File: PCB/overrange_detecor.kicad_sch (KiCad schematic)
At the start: 21 parts, among them Q105 BC807, Q301 BC807, U101 74HC00, U106 TLV3542, U7 TLV3542

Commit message: footprints
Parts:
- removed U106, U7: TLV3542, w-ic:SOIC-8, symbol w-analog-ic:TLV3542
- added C302: 100n, Capacitor_SMD:C_0603_1608Metric, symbol Device:C
- added U301: TLV3542, w-ic:SOIC-8, symbol w-analog-ic:TLV3542
- added U303: LM321, w-ic:SOT-23-5L, symbol w-analog-ic:LM321
- C301: renamed from C14; footprint (none) -> Capacitor_SMD:C_0603_1608Metric
- D301: footprint (none) -> LED_SMD:LED_0603_1608Metric
- R301: renamed from R110; footprint (none) -> Resistor_SMD:R_0603_1608Metric
- R302: renamed from R111; footprint (none) -> Resistor_SMD:R_0603_1608Metric
- R303: renamed from R113; footprint (none) -> Resistor_SMD:R_0603_1608Metric
- R304: renamed from R114; footprint (none) -> Resistor_SMD:R_0603_1608Metric
- R305: renamed from R112; footprint (none) -> Resistor_SMD:R_0603_1608Metric
- R306: renamed from R115; footprint (none) -> Resistor_SMD:R_0603_1608Metric
- R307: renamed from R301; footprint (none) -> Resistor_SMD:R_0603_1608Metric
- R308: renamed from R304; footprint (none) -> Resistor_SMD:R_0603_1608Metric
- R309: renamed from R302; footprint (none) -> Resistor_SMD:R_0603_1608Metric
- R310: renamed from R303; footprint (none) -> Resistor_SMD:R_0603_1608Metric
- R311: renamed from R5; footprint (none) -> Resistor_SMD:R_0603_1608Metric
- R312: renamed from R116; footprint (none) -> Resistor_SMD:R_0603_1608Metric
- R313: renamed from R4; footprint (none) -> Resistor_SMD:R_0603_1608Metric
- R314: renamed from R305; footprint (none) -> Resistor_SMD:R_0603_1608Metric
- U302: renamed from U101; footprint (none) -> w-ic:SOIC-14 208mil
- renumbered Q105 to Q301, Q301 to Q302
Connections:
- net +5V: now also C302.1, U303.2 (V-)
- net GND: now also C302.2, U303.5 (V+)
- net GNDA: now also U301.5 (+)
- net at D301.1 (K), R312.2, R313.1: now also U303.4
- net at C301.1, R309.2, R310.2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: now also U303.3 (-)
- net at R311.2, R313.2: now also U303.1 (+)
- net at R302.2, R304.1: now also U301.7
- net at R301.2, R302.1: now also U301.6 (-)
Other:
- moved on the sheet: C301, D301, Q301, Q302, R301, R302, R303, R304, R305, R306, R307, R308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

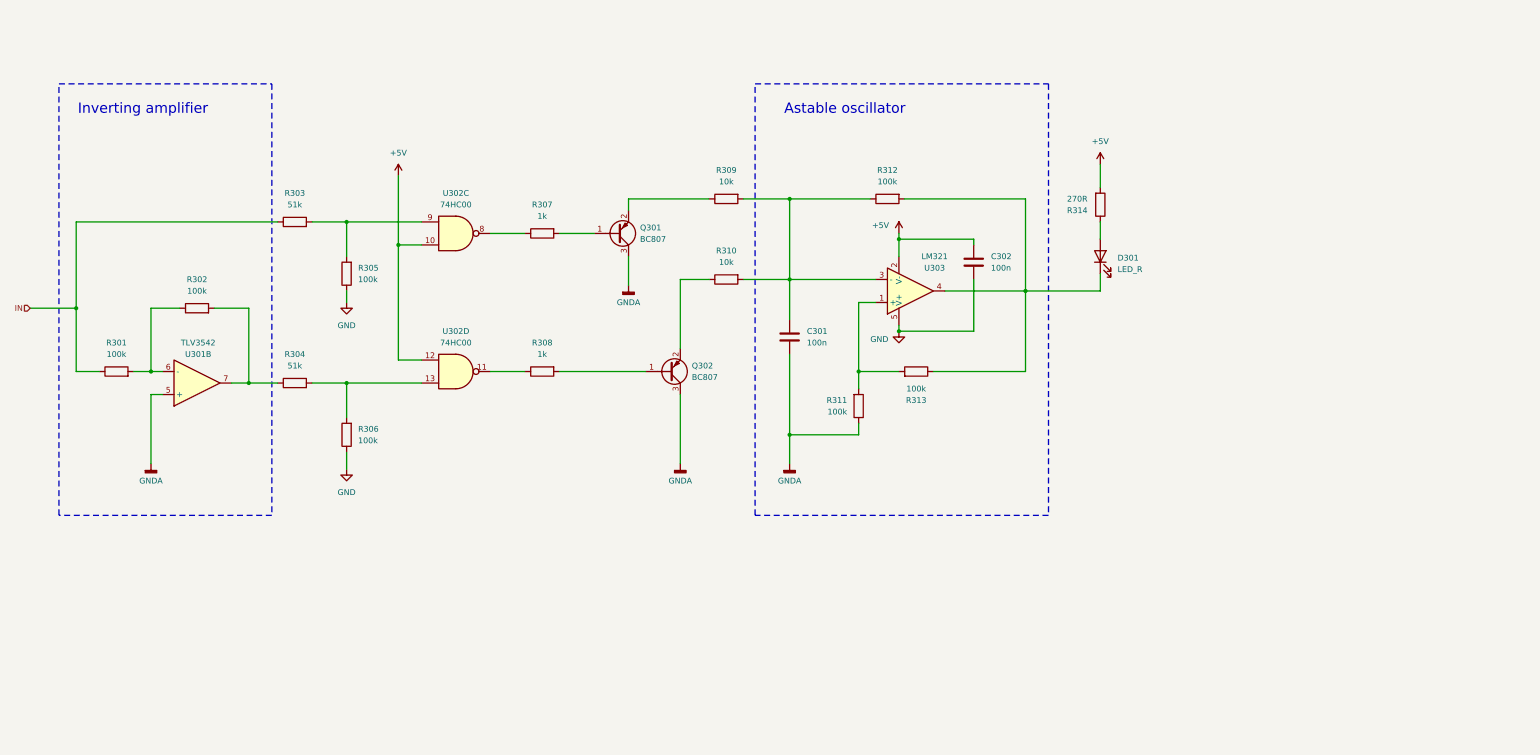
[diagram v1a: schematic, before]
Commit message: footprints and overrange detector timing
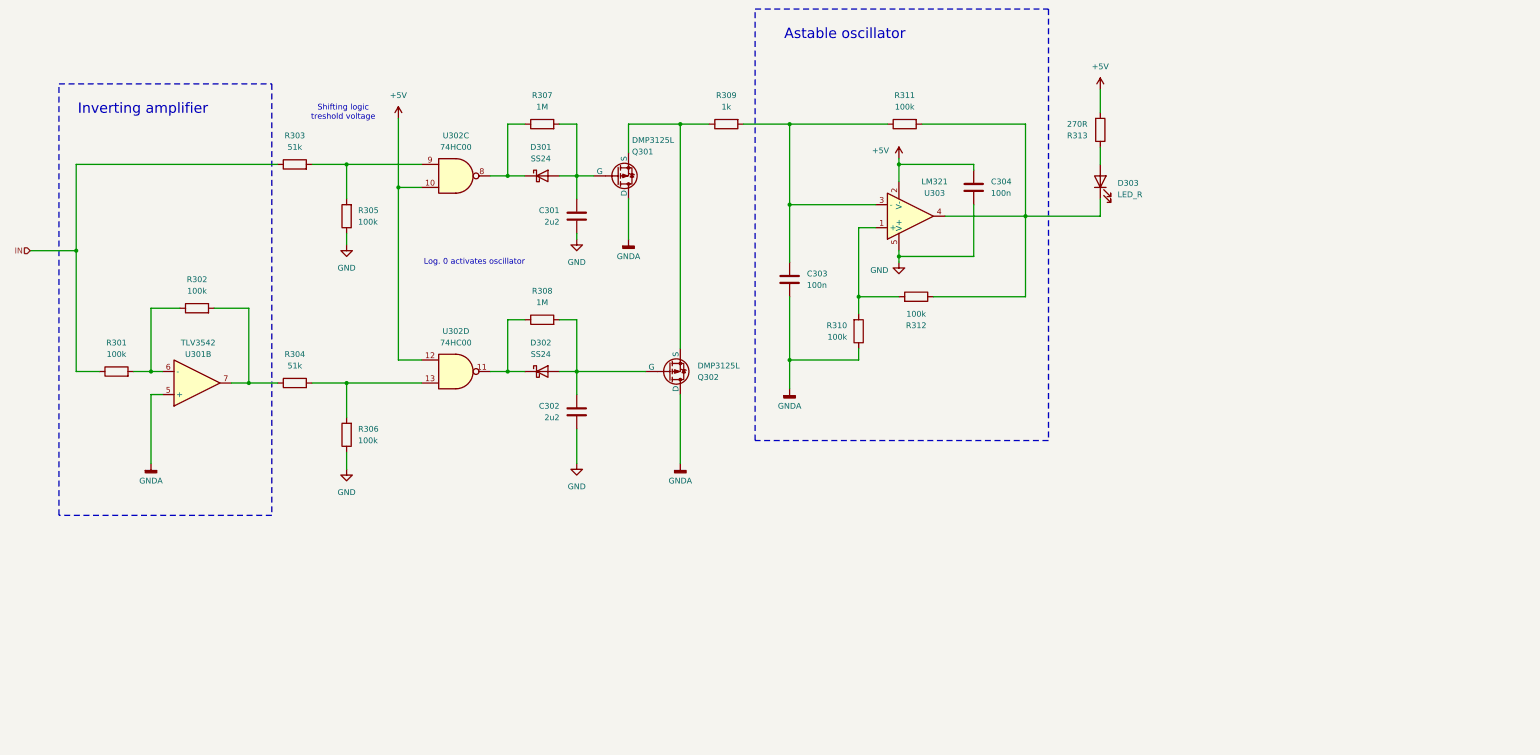
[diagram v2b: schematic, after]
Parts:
- removed Q301, Q302: BC807, w-ic:SOT-23, symbol Transistor_BJT:BC807
- removed R310: 10k, Resistor_SMD:R_0603_1608Metric, symbol Device:R
- added C301, C302: 2u2, Capacitor_SMD:C_0603_1608Metric, symbol Device:C
- added D301, D302: SS24, Diode_SMD:D_SMA, symbol Diode:SS24
- added Q301, Q302: DMP3125L, w-transistor:SOT23-3, symbol Simulation_SPICE:PMOS
- R307, R308: value 1k -> 1M
- R309: value 10k -> 1k
- renumbered C301 to C303, C302 to C304, D301 to D303, R311 to R310, R312 to R311, R313 to R312, R314 to R313
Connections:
- net GND: now also C301.2, C302.2
- net GNDA: now also Q301.2 (D), Q302.2 (D)
- net at R308.1, U302.11: now also D302.1 (K)
- net at R308.2: now also C302.1, D302.2 (A), Q302.1 (G)
- net at R307.2: now also C301.1, D301.2 (A), Q301.1 (G)
- net at R309.1: now also Q301.3 (S), Q302.3 (S)
- net at R307.1, U302.8: now also D301.1 (K)
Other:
- note added: "Log. 0 activates oscillator"
- note added: "Shifting logic treshold voltage"
- moved on the sheet: C303, C304, D303, R303, R305, R309, R310, R311, R312, R313, U302C, U303

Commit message: changes
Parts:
- removed U301: TLV3542, w-ic:SOIC-8, symbol w-analog-ic:TLV3542
- removed U302: 74HC00, w-ic:SOIC-14 208mil, symbol 74xx:74HC00
- added C303: 2u2, Capacitor_SMD:C_0603_1608Metric, symbol Device:C
- added U106: 74HC00, w-ic:SOIC-14 3.9x8.6mm P1.27mm, symbol 74xx:74HC00
- added U301: LM321, w-ic:SOT-23-5L, symbol w-analog-ic:LM321
- C301: value 2u2 -> 100n
- D301, D302: footprint Diode_SMD:D_SMA -> w-diode:SOD-123LF
- renumbered C303 to C304, C304 to C305, U303 to U302
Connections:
- net +5V: now also U106.10, U106.12
- net GND: now also C303.2, U301.5 (V+)
- net GNDA: now also U301.1 (+)
- net at D302.1 (K), R308.1: now also U106.11
- net -OR: now reaches D302.2 (A), Q302.1 (G), R308.2
- net -OR: now also C303.1; no longer C302.1
- net at R303.2, R305.2: now also U106.9
- net +OR: now reaches D301.2 (A), Q301.1 (G), R307.2
- net +OR: now also C302.1; no longer C301.1
- net at D301.1 (K), R307.1: now also U106.8
- net at R304.2, R306.2: now also U106.13
- net at R302.2, R304.1: now also U301.4
- net at R301.2, R302.1: now also U301.3 (-)
- new net +5VA: C301.1, U301.2 (V-)
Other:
- moved on the sheet: C304, C305, D303, Q301, Q302, R301, R302, R303, R304, R305, R306, R309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

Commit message: start of layout
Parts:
- D303: footprint LED_SMD:LED_0603_1608Metric -> LED_THT:LED_D3.0mm
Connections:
- net OR_OUT: now reaches D303.1 (K), R311.2, R312.1, U302.4
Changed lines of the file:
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@@
+		)
+	)
+	(label "OR_OUT"
+		(at 337.82 130.81 0)
+		(effects
+			(font
+				(size 1.27 1.27)
+			)
+			(justify left bottom)
 		)
 	)
@@
 			)
 		)
-		(property "Footprint" "LED_SMD:LED_0603_1608Metric"
+		(property "Footprint" "LED_THT:LED_D3.0mm"
 			(at 350.52 123.19 0)
 			(effects

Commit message: rough layout done
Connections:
- net +5V: now also U302.5 (V-); no longer U302.2 (V-)
- net GND: now also U302.2 (V+); no longer U302.5 (V+)
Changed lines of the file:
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@@
 	)
 	(symbol
+		(lib_name "LM321_1")
 		(lib_id "w-analog-ic:LM321")
 		(at 299.72 130.81 0)

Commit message: almost done
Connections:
- net +5V: now also D303.2 (A); no longer R313.2
- net OR_OUT: now also R313.1; no longer D303.1 (K)
- new net: D303.1 (K), R313.2
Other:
- moved on the sheet: D303, R313
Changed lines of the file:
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@@
+	(wire
+		(pts
+			(xy 350.52 125.73) (xy 350.52 130.81)
+		)
+		(stroke
+			(width 0)
+			(type default)
+		)
+	)
 	(wire
 		(pts
@@
 	(wire
 		(pts
-			(xy 350.52 127) (xy 350.52 130.81)
-		)
-		(stroke
-			(width 0)
-			(type default)
-		)
-	)
-	(wire
-		(pts
-			(xy 350.52 102.87) (xy 350.52 107.95)
+			(xy 350.52 114.3) (xy 350.52 118.11)
 		)
 		(stroke
@@
 	(wire
 		(pts
-			(xy 350.52 115.57) (xy 350.52 119.38)
-		)
-		(stroke
-			(width 0)
-			(type default)
-		)
-	)
-	(wire
-		(pts
 			(xy 62.23 139.7) (xy 81.28 139.7)
 		)
@@
 		(pts
 			(xy 299.72 119.38) (xy 299.72 123.19)
+		)
+		(stroke
+			(width 0)
+			(type default)
+		)
+	)
+	(wire
+		(pts
+			(xy 350.52 106.68) (xy 350.52 102.87)
 		)
 		(stroke
@@
 	(symbol
 		(lib_id "Device:LED")
-		(at 350.52 123.19 270)
+		(at 350.52 110.49 270)
 		(mirror x)
 		(unit 1)
@@
 		(dnp no)
 		(property "Reference" "D303"
-			(at 345.948 121.92 90)
+			(at 345.948 109.22 90)
 			(effects
 				(font
@@
 		)
 		(property "Value" "LED_R"
-			(at 345.948 124.46 90)
+			(at 345.948 111.76 90)
 			(effects
 				(font
@@
 		)
 		(property "Footprint" "LED_THT:LED_D3.0mm"
-			(at 350.52 123.19 0)
+			(at 350.52 110.49 0)
 			(effects
 				(font
@@
 		)
 		(property "Datasheet" "~"
-			(at 350.52 123.19 0)
+			(at 350.52 110.49 0)
 			(effects
 				(font
@@
 		)
 		(property "Description" "Light emitting diode"
-			(at 350.52 123.19 0)
+			(at 350.52 110.49 0)
 			(effects
 				(font
@@
 		)
 		(property "Sim.Pins" "1=K 2=A"
-			(at 350.52 123.19 0)
+			(at 350.52 110.49 0)
 			(effects
 				(font
@@
 	(symbol
 		(lib_id "Device:R")
-		(at 350.52 111.76 0)
+		(at 350.52 121.92 0)
 		(mirror x)
 		(unit 1)
@@
 		(dnp no)
 		(property "Reference" "R313"
-			(at 345.44 113.03 0)
+			(at 345.44 123.19 0)
 			(effects
 				(font
@@
 		)
 		(property "Value" "270R"
-			(at 345.44 110.49 0)
+			(at 345.44 120.65 0)
 			(effects
 				(font
@@
 		)
 		(property "Footprint" "Resistor_SMD:R_0603_1608Metric"
-			(at 348.742 111.76 90)
+			(at 348.742 121.92 90)
 			(effects
 				(font
@@
 		)
 		(property "Datasheet" "~"
-			(at 350.52 111.76 0)
+			(at 350.52 121.92 0)
 			(effects
 				(font
@@
 		)
 		(property "Description" "Resistor"
-			(at 350.52 111.76 0)
-			(effects
-				(font
+			(at 350.52 121.92 0)
+			(effects
+				(font
